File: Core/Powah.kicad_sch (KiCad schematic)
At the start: 36 parts, among them J20 Conn_02x08_Odd_Even, U10 TL072, U11 TL072, U12 TL072, U3 MIC5504-3.3YM5, U4 TL072, U5 TL072, U6 TL072, U7 TL072, U9 TL072

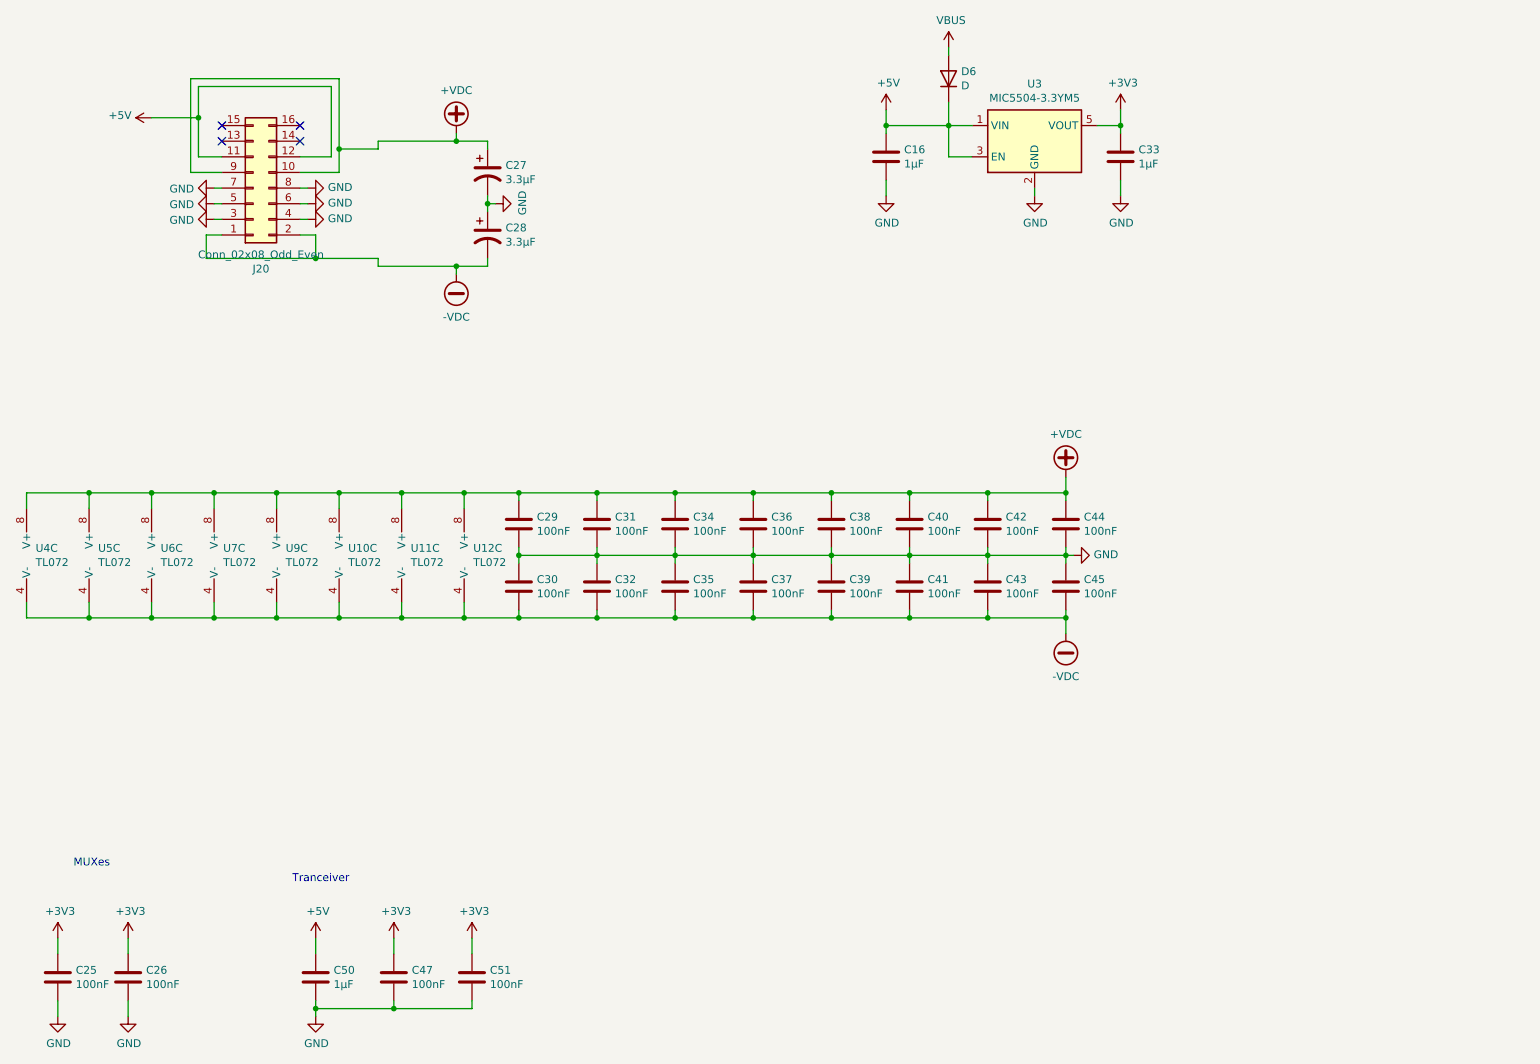
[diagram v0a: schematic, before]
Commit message: Update PCBs to V3.0
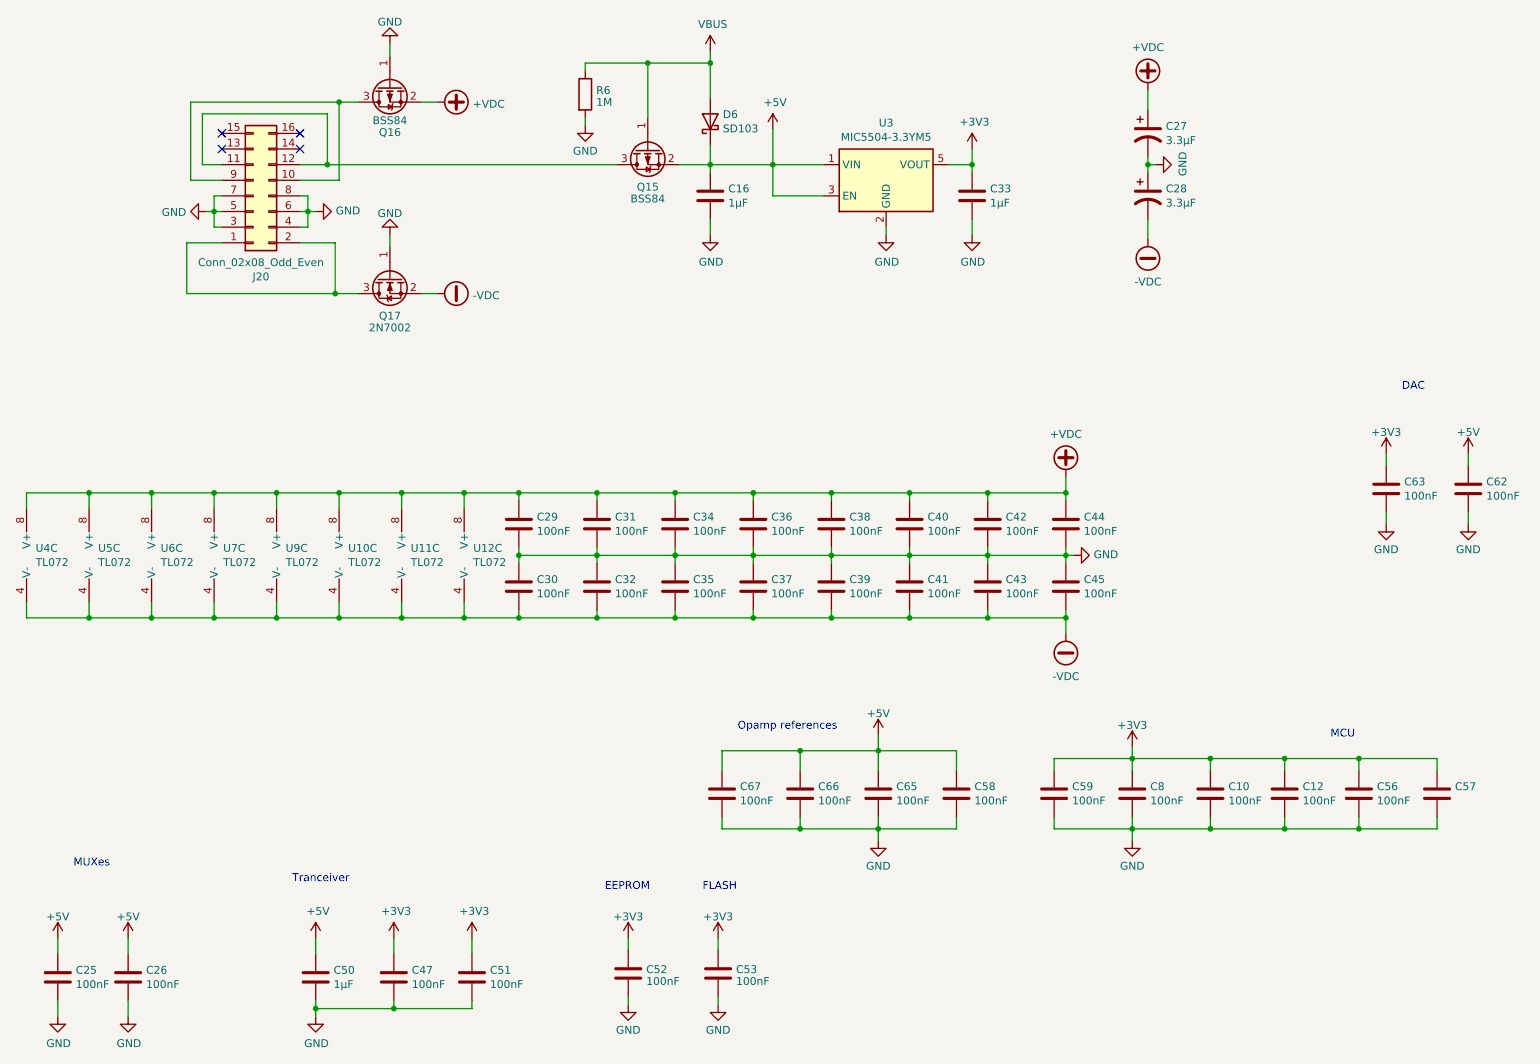
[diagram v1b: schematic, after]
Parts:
- added C10, C12, C52, C53, C56, C57, C58, C59, C62, C63, C65, C66, C67, C8: 100nF, Capacitor_SMD:C_0603_1608Metric, symbol Device:C
- added Q15, Q16: BSS84, Package_TO_SOT_SMD:SOT-23, symbol Transistor_FET:BSS84
- added Q17: 2N7002, Package_TO_SOT_SMD:SOT-23, symbol Transistor_FET:2N7002
- added R6: 1M, Resistor_SMD:R_0603_1608Metric, symbol Device:R
- D6: value D -> SD103; symbol Device:D -> Device:D_Schottky
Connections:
- net +3V3: now also C10.1, C12.1, C52.1, C53.1, C56.1, C57.1, C59.1, C63.1, C8.1; no longer C25.1, C26.1
- net +5V: now also C25.1, C26.1, C58.1, C62.1, C65.1, C66.1, C67.1, Q15.2 (S); no longer J20.11 (Pin_11), J20.12 (Pin_12)
- net +VDC: now also Q16.2 (S); no longer J20.10 (Pin_10), J20.9 (Pin_9)
- net -VDC: now also Q17.2 (S); no longer J20.1 (Pin_1), J20.2 (Pin_2)
- net GND: now also C10.2, C12.2, C52.2, C53.2, C56.2, C57.2, C58.2, C59.2, C62.2, C63.2, C65.2, C66.2, C67.2, C8.2, Q16.1 (G), Q17.1 (G), R6.2
- net VBUS: now also Q15.1 (G), R6.1
- new net: J20.1 (Pin_1), J20.2 (Pin_2), Q17.3 (D)
- new net: J20.10 (Pin_10), J20.9 (Pin_9), Q16.3 (D)
- new net: J20.11 (Pin_11), J20.12 (Pin_12), Q15.3 (D)
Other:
- note added: "DAC"
- note added: "EEPROM"
- note added: "FLASH"
- note added: "MCU"
- note added: "Opamp references"
- moved on the sheet: C16, C27, C28, C33, D6, J20, U3

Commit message: Minor fixes
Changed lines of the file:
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@@
   (title_block
     (title "M2IDI - CV16 CORE")
-    (date "2023-04-22")
+    (date "2023-05-10")
     (rev "3.0")
     (company "GuavTek")
@@
     )
     (property "Value" "100nF" (at 257.556 147.828 0)
-      (effects (font (size 1.27 1.27)) (justify left) hide)
+      (effects (font (size 1.27 1.27)) (justify left))
     )
     (property "Footprint" "Capacitor_SMD:C_0603_1608Metric" (at 255.6002 150.495 0)

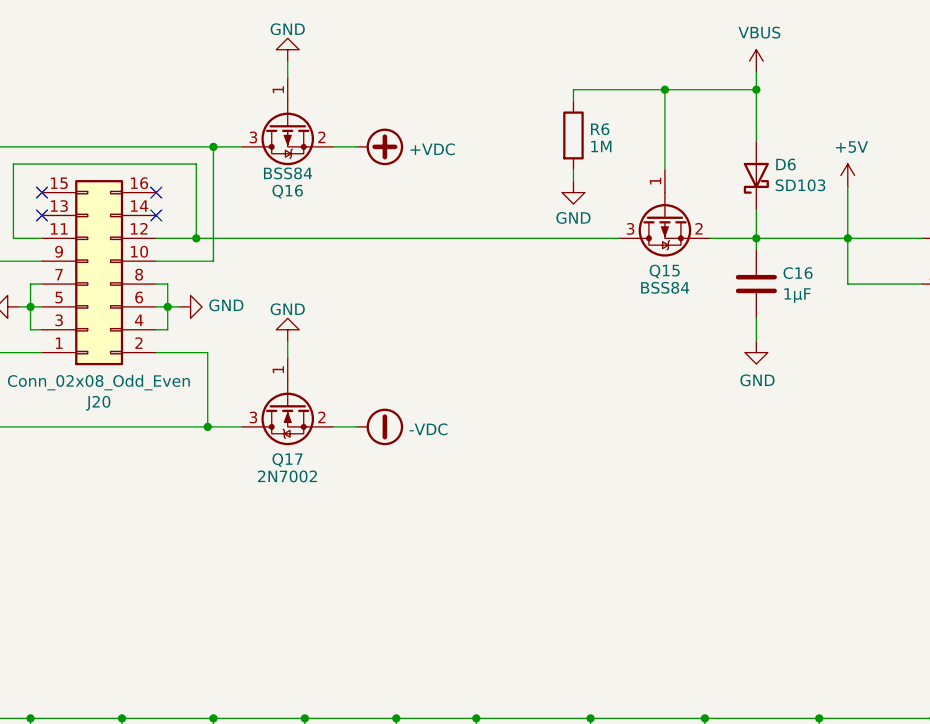
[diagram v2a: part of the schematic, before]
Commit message: Improve USB impedance and power headroom
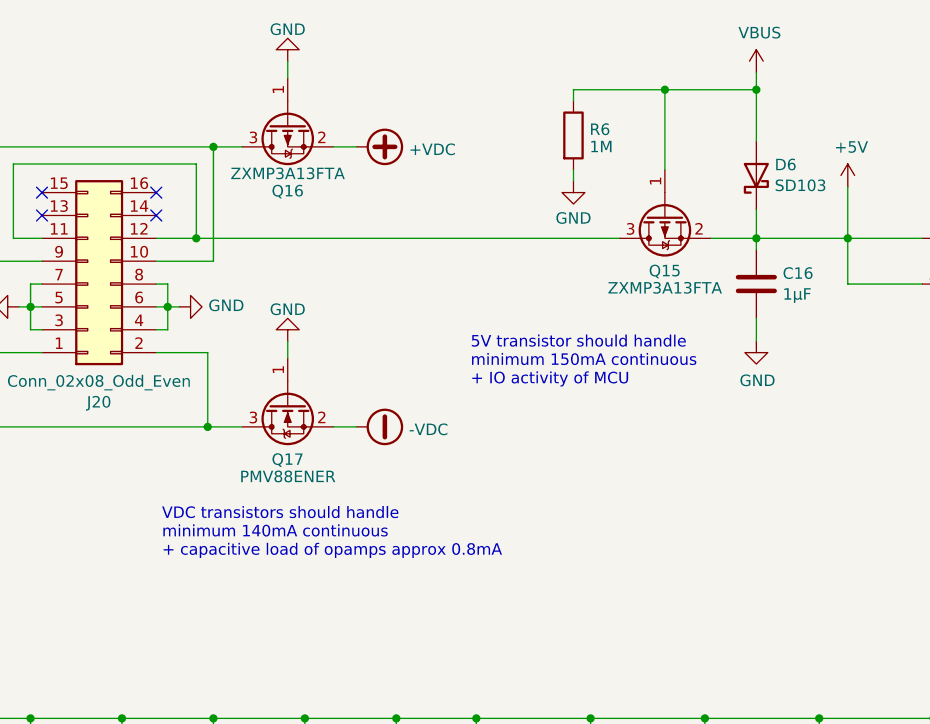
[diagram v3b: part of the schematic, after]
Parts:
- Q15, Q16: value BSS84 -> ZXMP3A13FTA
- Q17: value 2N7002 -> PMV88ENER
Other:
- note added: "5V transistor should handle minimum 150mA continuous + IO activity of MCU"
- note added: "VDC transistors should handle minimum 140mA continuous + capacitive load of opamps approx 0.8mA"
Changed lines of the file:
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@@
+    (effects (font (size 1.27 1.27)) (justify left bottom))
+  )
+  (text "VDC transistors should handle\nminimum 140mA continuous\n+ capacitive load of opamps approx 0.8mA"
+    (at 70.485 80.01 0)
     (effects (font (size 1.27 1.27)) (justify left bottom))
   )
@@
   (text "MCU" (at 241.3 137.795 0)
     (effects (font (size 1.27 1.27)) (justify right bottom))
+  )
+  (text "5V transistor should handle\nminimum 150mA continuous\n+ IO activity of MCU"
+    (at 104.775 60.96 0)
+    (effects (font (size 1.27 1.27)) (justify left bottom))
   )
   (text "FLASH" (at 135.255 162.56 0)
@@
       (effects (font (size 1.27 1.27)))
     )
-    (property "Value" "2N7002" (at 84.455 70.9535 90)
+    (property "Value" "PMV88ENER" (at 84.455 70.9535 90)
       (effects (font (size 1.27 1.27)))
     )
@@
       (effects (font (size 1.27 1.27)))
     )
-    (property "Value" "BSS84" (at 126.365 49.9985 90)
+    (property "Value" "ZXMP3A13FTA" (at 126.365 49.9985 90)
       (effects (font (size 1.27 1.27)))
     )
@@
       (effects (font (size 1.27 1.27)))
     )
-    (property "Value" "BSS84" (at 84.455 37.2839 90)
-      (effects (font (size 1.27 1.27)))
-    )
+    (property "Value" "ZXMP3A13FTA" (at 84.455 37.2839 90)
+      (effects (font (size 1.27 1.27)))
+    )

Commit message: Finalize module
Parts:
- removed C27, C28: 3.3µF, Capacitor_Tantalum_SMD:CP_EIA-3216-18_Kemet-A, symbol Device:C_Polarized_US
- added C27, C28: 10µF, Capacitor_SMD:C_0805_2012Metric, symbol Device:C
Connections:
- net +VDC: now also C27.1
- net -VDC: now also C28.2
- net GND: now also C27.2, C28.1
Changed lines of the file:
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@@
-    )
-  )
-  (symbol (lib_id "Device:C_Polarized_US") (at 207.645 39.37 0) (unit 1)
-    (in_bom yes) (on_board yes) (dnp no)
-    (property "Reference" "C27" (at 210.566 38.2016 0)
-      (effects (font (size 1.27 1.27)) (justify left))
-    )
-    (property "Value" "3.3µF" (at 210.566 40.513 0)
-      (effects (font (size 1.27 1.27)) (justify left))
-    )
-    (property "Footprint" "Capacitor_Tantalum_SMD:CP_EIA-3216-18_Kemet-A" (at 207.645 39.37 0)
-      (effects (font (size 1.27 1.27)) hide)
-    )
-    (property "Datasheet" "~" (at 207.645 39.37 0)
-      (effects (font (size 1.27 1.27)) hide)
-    )
-    (pin "1")
-    (pin "2")
-    (instances
-      (project "MIDI_CV16"
-        (path "/ba515087-2175-44fd-acc2-0e447df6195b"
-          (reference "C27") (unit 1)
-        )
-        (path "/ba515087-2175-44fd-acc2-0e447df6195b/00000000-0000-0000-0000-000060750bb0"
-          (reference "C27") (unit 1)
-        )
-      )
-    )
-  )
-  (symbol (lib_id "Device:C_Polarized_US") (at 207.645 49.53 0) (unit 1)
-    (in_bom yes) (on_board yes) (dnp no)
-    (property "Reference" "C28" (at 210.566 48.3616 0)
-      (effects (font (size 1.27 1.27)) (justify left))
-    )
-    (property "Value" "3.3µF" (at 210.566 50.673 0)
-      (effects (font (size 1.27 1.27)) (justify left))
-    )
-    (property "Footprint" "Capacitor_Tantalum_SMD:CP_EIA-3216-18_Kemet-A" (at 207.645 49.53 0)
-      (effects (font (size 1.27 1.27)) hide)
-    )
-    (property "Datasheet" "~" (at 207.645 49.53 0)
-      (effects (font (size 1.27 1.27)) hide)
-    )
-    (pin "1")
-    (pin "2")
-    (instances
-      (project "MIDI_CV16"
-        (path "/ba515087-2175-44fd-acc2-0e447df6195b"
-          (reference "C28") (unit 1)
-        )
-        (path "/ba515087-2175-44fd-acc2-0e447df6195b/00000000-0000-0000-0000-000060750bb0"
-          (reference "C28") (unit 1)
-        )
-      )
     )
   )
@@
     )
   )
+  (symbol (lib_id "Device:C") (at 207.645 49.53 0) (unit 1)
+    (in_bom yes) (on_board yes) (dnp no) (fields_autoplaced)
+    (property "Reference" "C28" (at 210.566 48.3179 0)
+      (effects (font (size 1.27 1.27)) (justify left))
+    )
+    (property "Value" "10µF" (at 210.566 50.7421 0)
+      (effects (font (size 1.27 1.27)) (justify left))
+    )
+    (property "Footprint" "Capacitor_SMD:C_0805_2012Metric" (at 208.6102 53.34 0)
+      (effects (font (size 1.27 1.27)) hide)
+    )
+    (property "Datasheet" "~" (at 207.645 49.53 0)
+      (effects (font (size 1.27 1.27)) hide)
+    )
+    (pin "1")
+    (pin "2")
+    (instances
+      (project "MIDI_CV16"
+        (path "/ba515087-2175-44fd-acc2-0e447df6195b/00000000-0000-0000-0000-000060750bb0"
+          (reference "C28") (unit 1)
+        )
+      )
+    )
+  )
   (symbol (lib_id "Device:C") (at 259.715 97.155 0) (unit 1)
     (in_bom yes) (on_board yes) (dnp no)
@@
         )
       )
+    )
+  )
+  (symbol (lib_id "Device:C") (at 207.645 39.37 0) (unit 1)
+    (in_bom yes) (on_board yes) (dnp no) (fields_autoplaced)
+    (property "Reference" "C27" (at 210.566 38.1579 0)
+      (effects (font (size 1.27 1.27)) (justify left))
+    )
+    (property "Value" "10µF" (at 210.566 40.5821 0)
+      (effects (font (size 1.27 1.27)) (justify left))
+    )
+    (property "Footprint" "Capacitor_SMD:C_0805_2012Metric" (at 208.6102 43.18 0)
+      (effects (font (size 1.27 1.27)) hide)
+    )
+    (property "Datasheet" "~" (at 207.645 39.37 0)
+      (effects (font (size 1.27 1.27)) hide)
+    )
+    (pin "1")
+    (pin "2")
+    (instances
+      (project "MIDI_CV16"
+        (path "/ba515087-2175-44fd-acc2-0e447df6195b/00000000-0000-0000-0000-000060750bb0"
+          (reference "C27") (unit 1)
+        )
+      )
